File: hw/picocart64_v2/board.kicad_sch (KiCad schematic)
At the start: 80 parts, among them J1 USB_C_Receptacle_USB2.0, J2 USB_C_Receptacle_USB2.0, J3 Conn_02x06_Odd_Even, J4 Micro_SD_Card_Det, J5 Conn_01x02, J6 Conn_01x06, Q1 FDN340P, SW1 BootButton, U10 USBLC6-2SC6, U11 AZ1117-3.3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

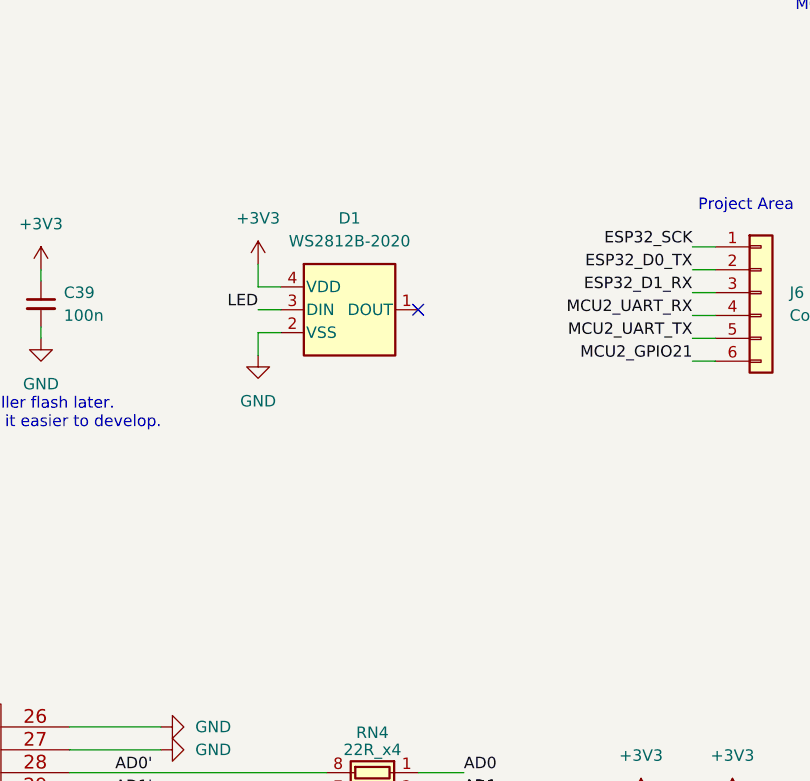
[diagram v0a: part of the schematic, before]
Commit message: hw: picocart64_v2: Added alternative LED and pin 1 markings
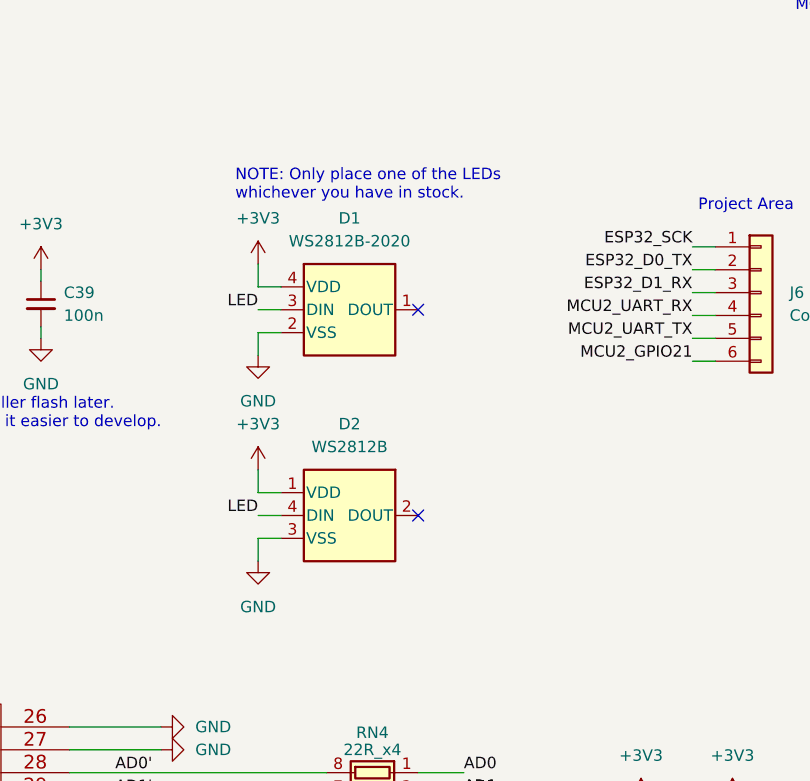
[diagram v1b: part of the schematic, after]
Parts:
- added D2: WS2812B, LED_SMD:LED_WS2812B_PLCC4_5.0x5.0mm_P3.2mm, symbol LED_Extra:WS2812B
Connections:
- net +3V3: now also D2.1 (VDD)
- net GND: now also D2.3 (VSS)
- net LED: now also D2.4 (DIN)
- no-connect marks 24 -> 25
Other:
- note added: "NOTE: Only place one of the LEDs whichever you have in stock."
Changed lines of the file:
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@@
   (no_connect (at 375.92 205.74))
   (no_connect (at 120.015 245.745))
+  (no_connect (at 158.75 191.77))
   (no_connect (at 321.31 208.28))
   (no_connect (at 41.91 146.05))
@@
     (stroke (width 0) (type default) (color 0 0 0 0))
   )
+  (wire (pts (xy 140.97 194.31) (xy 143.51 194.31))
+    (stroke (width 0) (type default) (color 0 0 0 0))
+  )
   (wire (pts (xy 58.42 68.58) (xy 59.69 68.58))
     (stroke (width 0) (type default) (color 0 0 0 0))
@@
     (stroke (width 0) (type default) (color 0 0 0 0))
   )
+  (wire (pts (xy 140.97 191.77) (xy 143.51 191.77))
+    (stroke (width 0) (type default) (color 0 0 0 0))
+  )
   (wire (pts (xy 163.83 34.29) (xy 170.18 34.29))
     (stroke (width 0) (type default) (color 0 0 0 0))
@@
     (stroke (width 0) (type default) (color 0 0 0 0))
   )
+  (wire (pts (xy 140.97 189.23) (xy 143.51 189.23))
+    (stroke (width 0) (type default) (color 0 0 0 0))
+  )
   (wire (pts (xy 227.965 234.95) (xy 233.045 234.95))
     (stroke (width 0) (type default) (color 0 0 0 0))
@@
     (stroke (width 0) (type default) (color 0 0 0 0))
   )
+  (wire (pts (xy 140.97 196.85) (xy 140.97 194.31))
+    (stroke (width 0) (type default) (color 0 0 0 0))
+  )
   (wire (pts (xy 201.93 46.99) (xy 204.47 46.99))
     (stroke (width 0) (type default) (color 0 0 0 0))
@@
     (stroke (width 0) (type default) (color 0 0 0 0))
   )
+  (wire (pts (xy 140.97 186.69) (xy 140.97 189.23))
+    (stroke (width 0) (type default) (color 0 0 0 0))
+  )
   (wire (pts (xy 171.45 123.19) (xy 171.45 120.65))
     (stroke (width 0) (type default) (color 0 0 0 0))
@@
     (effects (font (size 1.27 1.27)) (justify left bottom))
   )
+  (text "NOTE: Only place one of the LEDs\nwhichever you have in stock."
+    (at 138.43 156.845 0)
+    (effects (font (size 1.27 1.27)) (justify left bottom))
+  )
   (text "[PIO#1]" (at 383.54 52.07 0)
     (effects (font (size 1.27 1.27)) (justify left bottom))
@@
     (effects (font (size 1.27 1.27)) (justify left bottom))
   )
+  (label "LED" (at 140.97 191.77 180)
+    (effects (font (size 1.27 1.27)) (justify right bottom))
+  )
   (label "~{INT1}" (at 204.47 102.87 0)
     (effects (font (size 1.27 1.27)) (justify left bottom))
@@
     (pin "2")
   )
+  (symbol (lib_id "power:+3V3") (at 140.97 186.69 0) (unit 1)
+    (in_bom yes) (on_board yes) (fields_autoplaced)
+    (property "Reference" "#PWR0116" (id 0) (at 140.97 190.5 0)
+      (effects (font (size 1.27 1.27)) hide)
+    )
+    (property "Value" "+3V3" (id 1) (at 140.97 181.61 0))
+    (property "Footprint" "" (id 2) (at 140.97 186.69 0)
+      (effects (font (size 1.27 1.27)) hide)
+    )
+    (property "Datasheet" "" (id 3) (at 140.97 186.69 0)
+      (effects (font (size 1.27 1.27)) hide)
+    )
+    (pin "1")
+  )
   (symbol (lib_id "power:GND") (at 129.54 26.67 0) (unit 1)
     (in_bom yes) (on_board yes)
@@
     (pin "2")
   )
+  (symbol (lib_id "power:GND") (at 140.97 196.85 0) (unit 1)
+    (in_bom yes) (on_board yes) (fields_autoplaced)
+    (property "Reference" "#PWR0117" (id 0) (at 140.97 203.2 0)
+      (effects (font (size 1.27 1.27)) hide)
+    )
+    (property "Value" "GND" (id 1) (at 140.97 201.93 0))
+    (property "Footprint" "" (id 2) (at 140.97 196.85 0)
+      (effects (font (size 1.27 1.27)) hide)
+    )
+    (property "Datasheet" "" (id 3) (at 140.97 196.85 0)
+      (effects (font (size 1.27 1.27)) hide)
+    )
+    (pin "1")
+  )
   (symbol (lib_id "Connector:TestPoint") (at 227.33 120.65 270) (unit 1)
     (in_bom yes) (on_board yes) (fields_autoplaced)
@@
       (effects (font (size 1.27 1.27)) hide)
     )
+    (pin "1")
+    (pin "2")
+    (pin "3")
+    (pin "4")
+  )
+  (symbol (lib_id "LED_Extra:WS2812B") (at 151.13 191.77 0) (unit 1)
+    (in_bom yes) (on_board yes) (fields_autoplaced)
+    (property "Reference" "D2" (id 0) (at 151.13 181.61 0))
+    (property "Value" "WS2812B" (id 1) (at 151.13 184.15 0))
+    (property "Footprint" "LED_SMD:LED_WS2812B_PLCC4_5.0x5.0mm_P3.2mm" (id 2) (at 151.13 200.66 0)
+      (effects (font (size 1.27 1.27)) hide)
+    )
+    (property "Datasheet" "https://cdn-shop.adafruit.com/datasheets/WS2812B.pdf" (id 3) (at 152.4 203.2 0)
+      (effects (font (size 1.27 1.27)) hide)
+    )
